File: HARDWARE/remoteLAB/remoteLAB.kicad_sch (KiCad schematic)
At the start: 0 parts

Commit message: add: create schematic files for MCU, TFT, Analog In, Analog Out, Bluetooth, Ethernet, and USBC
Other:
- added sheet Analog input (analog_in.kicad_sch)
- added sheet Analog output (analog_out.kicad_sch)
- added sheet Bluetooth (bluetooth.kicad_sch)
- added sheet Ethernet (ethernet.kicad_sch)
- added sheet MCU (MCU.kicad_sch)
- added sheet TFT (TFT.kicad_sch)
- added sheet USBC (usbc.kicad_sch)

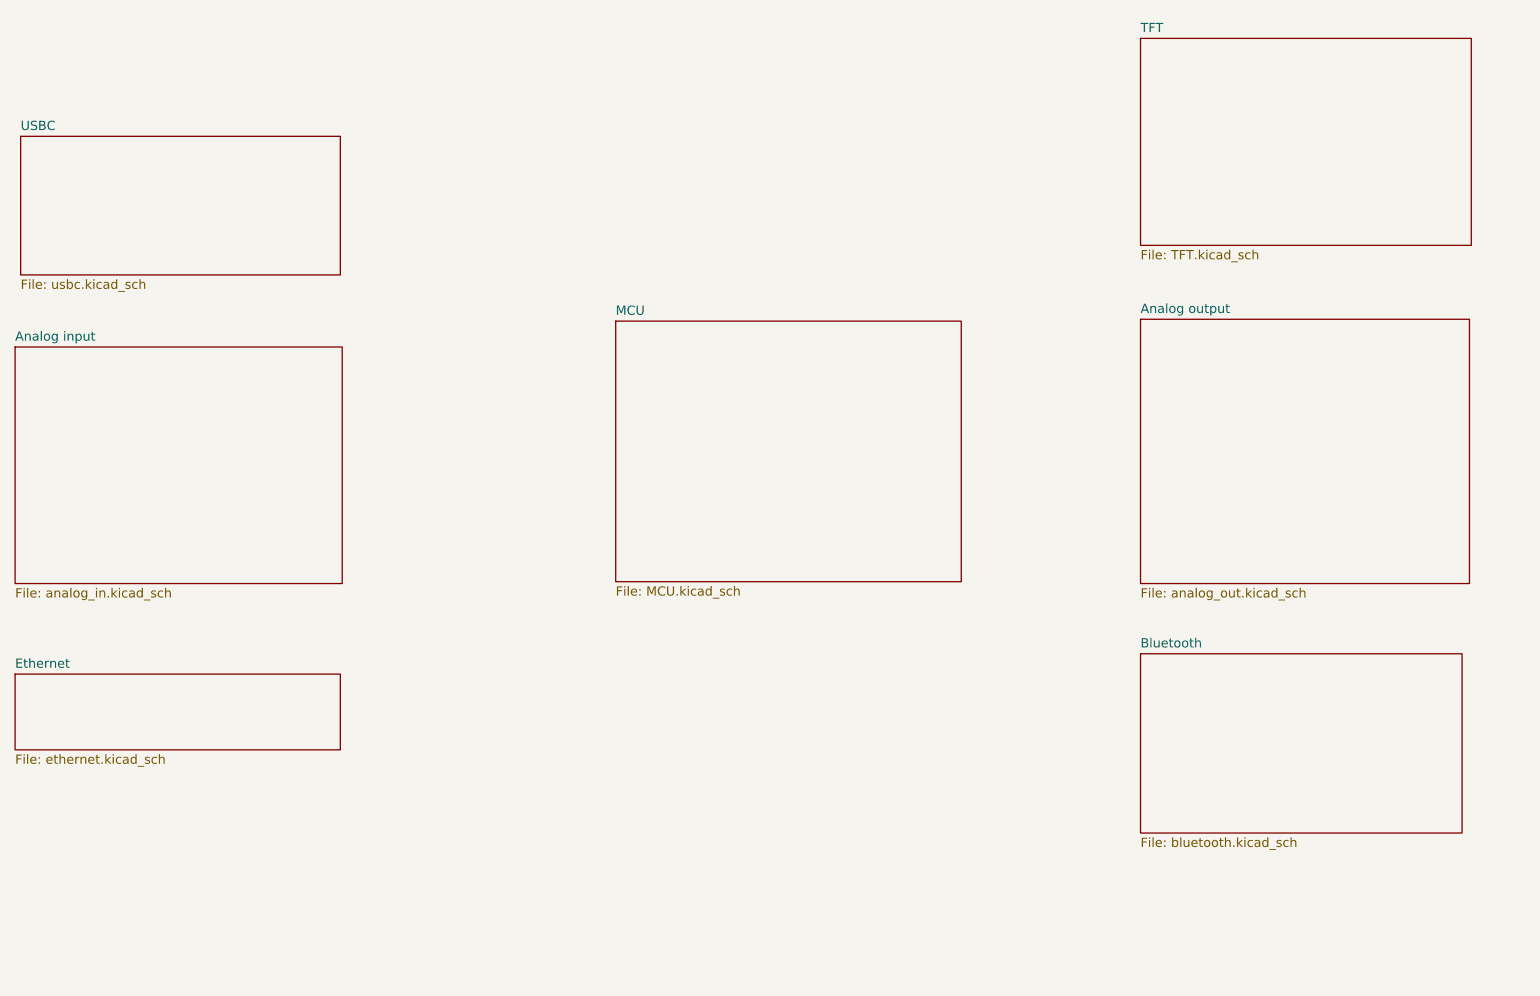
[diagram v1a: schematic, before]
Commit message: added symbols for display connector and BT part, added usb device to ioc
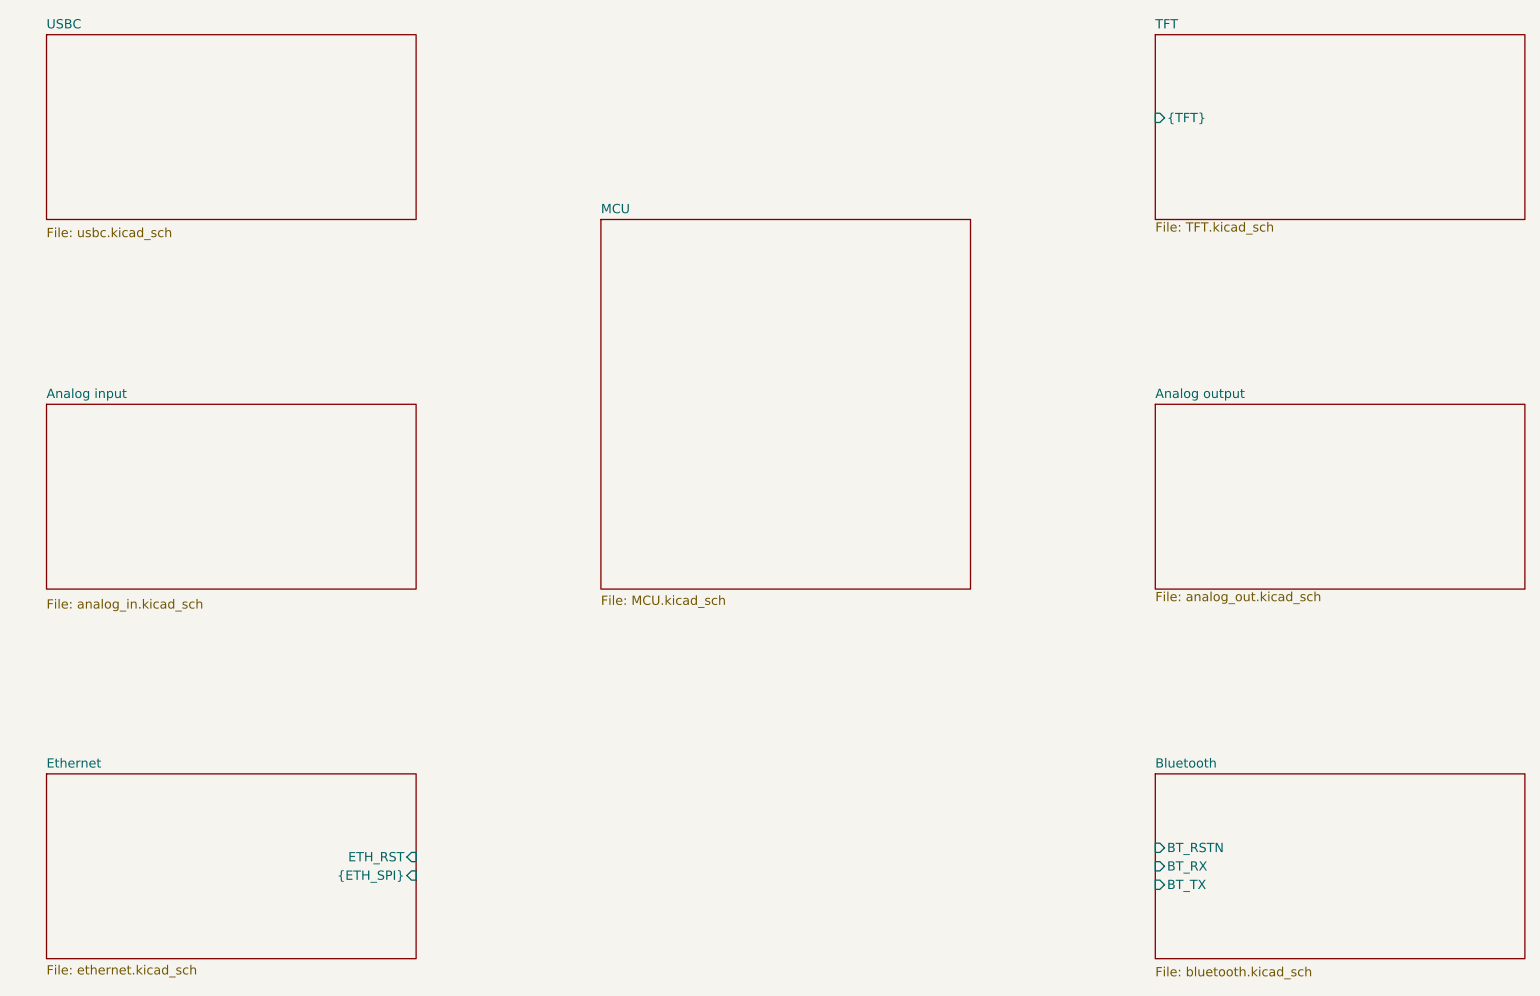
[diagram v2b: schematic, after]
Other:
- sheet Bluetooth ports: added BT_RSTN, BT_RX, BT_TX; removed none
- sheet Ethernet ports: added ETH_RST, {ETH_SPI}; removed none
- sheet TFT ports: added {TFT}; removed none
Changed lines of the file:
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@@
 	(paper "A4")
 	(sheet
-		(at 47.244 39.37)
-		(size 43.942 19.05)
+		(at 50.8 25.4)
+		(size 50.8 25.4)
 		(exclude_from_sim no)
 		(in_bom yes)
@@
 		)
 		(property "Sheetname" "USBC"
-			(at 47.244 38.6584 0)
+			(at 50.8 24.6884 0)
 			(show_name no)
 			(do_not_autoplace no)
@@
 		)
 		(property "Sheetfile" "usbc.kicad_sch"
-			(at 47.244 59.0046 0)
+			(at 50.8 51.8926 0)
 			(show_name no)
 			(do_not_autoplace no)
@@
 	)
 	(sheet
-		(at 201.168 110.49)
-		(size 44.196 24.638)
+		(at 203.2 127)
+		(size 50.8 25.4)
 		(exclude_from_sim no)
 		(in_bom yes)
@@
 		)
 		(property "Sheetname" "Bluetooth"
-			(at 201.168 109.7784 0)
+			(at 203.2 126.2884 0)
 			(show_name no)
 			(do_not_autoplace no)
@@
 		)
 		(property "Sheetfile" "bluetooth.kicad_sch"
-			(at 201.168 135.7126 0)
+			(at 203.2 153.4926 0)
 			(show_name no)
 			(do_not_autoplace no)
@@
 		)
 		(property "Field2" ""
-			(at 201.168 110.49 0)
+			(at 203.2 127 0)
 			(hide yes)
 			(show_name no)
@@
 			)
 		)
+		(pin "BT_RSTN" input
+			(at 203.2 137.16 180)
+			(effects
+				(font
+					(size 1.27 1.27)
+				)
+				(justify left)
+			)
+		)
+		(pin "BT_RX" input
+			(at 203.2 139.7 180)
+			(effects
+				(font
+					(size 1.27 1.27)
+				)
+				(justify left)
+			)
+		)
+		(pin "BT_TX" input
+			(at 203.2 142.24 180)
+			(effects
+				(font
+					(size 1.27 1.27)
+				)
+				(justify left)
+			)
+		)
 		(instances
 			(project "remoteLAB"
@@
 	)
 	(sheet
-		(at 201.168 64.516)
-		(size 45.212 36.322)
+		(at 203.2 76.2)
+		(size 50.8 25.4)
 		(exclude_from_sim no)
 		(in_bom yes)
@@
 		)
 		(property "Sheetname" "Analog output"
-			(at 201.168 63.8044 0)
+			(at 203.2 75.4884 0)
 			(show_name no)
 			(do_not_autoplace no)
@@
 		)
 		(property "Sheetfile" "analog_out.kicad_sch"
-			(at 201.168 101.4226 0)
+			(at 203.2 101.9306 0)
 			(show_name no)
 			(do_not_autoplace no)
@@
 	)
 	(sheet
-		(at 46.482 68.326)
-		(size 44.958 32.512)
+		(at 50.8 76.2)
+		(size 50.8 25.4)
 		(exclude_from_sim no)
 		(in_bom yes)
@@
 		)
 		(property "Sheetname" "Analog input"
-			(at 46.482 67.6144 0)
+			(at 50.8 75.4884 0)
 			(show_name no)
 			(do_not_autoplace no)
@@
 		)
 		(property "Sheetfile" "analog_in.kicad_sch"
-			(at 46.482 101.4226 0)
+			(at 50.8 102.9466 0)
 			(show_name no)
 			(do_not_autoplace no)
@@
 	)
 	(sheet
-		(at 129.032 64.77)
-		(size 47.498 35.814)
+		(at 127 50.8)
+		(size 50.8 50.8)
 		(exclude_from_sim no)
 		(in_bom yes)
@@
 		)
 		(property "Sheetname" "MCU"
-			(at 129.032 64.0584 0)
+			(at 127 50.0884 0)
 			(show_name no)
 			(do_not_autoplace no)
@@
 		)
 		(property "Sheetfile" "MCU.kicad_sch"
-			(at 129.032 101.1686 0)
+			(at 127 102.4386 0)
 			(show_name no)
 			(do_not_autoplace no)
@@
 	)
 	(sheet
-		(at 201.168 25.908)
-		(size 45.466 28.448)
+		(at 203.2 25.4)
+		(size 50.8 25.4)
 		(exclude_from_sim no)
 		(in_bom yes)
@@
 		)
 		(property "Sheetname" "TFT"
-			(at 201.168 25.1964 0)
+			(at 203.2 24.6884 0)
 			(show_name no)
 			(do_not_autoplace no)
@@
 		)
 		(property "Sheetfile" "TFT.kicad_sch"
-			(at 201.168 54.9406 0)
-			(show_name no)
-			(do_not_autoplace no)
-			(effects
-				(font
-					(size 1.27 1.27)
-				)
-				(justify left top)
+			(at 203.2 51.1306 0)
+			(show_name no)
+			(do_not_autoplace no)
+			(effects
+				(font
+					(size 1.27 1.27)
+				)
+				(justify left top)
+			)
+		)
+		(pin "{TFT}" input
+			(at 203.2 36.83 180)
+			(effects
+				(font
+					(size 1.27 1.27)
+				)
+				(justify left)
 			)
 		)
@@
 	)
 	(sheet
-		(at 46.482 113.284)
-		(size 44.704 10.414)
+		(at 50.8 127)
+		(size 50.8 25.4)
 		(exclude_from_sim no)
 		(in_bom yes)
@@
 		)
 		(property "Sheetname" "Ethernet"
-			(at 46.482 112.5724 0)
+			(at 50.8 126.2884 0)
 			(show_name no)
 			(do_not_autoplace no)
@@
 		)
 		(property "Sheetfile" "ethernet.kicad_sch"
-			(at 46.482 124.2826 0)
-			(show_name no)
-			(do_not_autoplace no)
-			(effects
-				(font
-					(size 1.27 1.27)
-				)
-				(justify left top)
-			)
-		)
+			(at 50.8 153.2386 0)
+			(show_name no)
+			(do_not_autoplace no)
+			(effects
+				(font
+					(size 1.27 1.27)
+				)
+				(justify left top)
+			)
+		)
+		(pin "ETH_RST" input
+			(at 101.6 138.43 0)
+			(effects
+				(font
+					(size 1.27 1.27)
+				)
+				(justify right)
+			)
+		)
+		(pin "{ETH_SPI}" input
+			(at 101.6 140.97 0)
+			(effects
+				(font
+					(size 1.27 1.27)
+				)
+				(justify right)
+			)
+		)

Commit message: usb power isolation and input
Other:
- sheet USBC ports: added DD+, DD-; removed none
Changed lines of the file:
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@@
+			)
+		)
+		(pin "DD+" input
+			(at 101.6 34.29 0)
+			(effects
+				(font
+					(size 1.27 1.27)
+				)
+				(justify right)
+			)
+		)
+		(pin "DD-" input
+			(at 101.6 36.83 0)
+			(effects
+				(font
+					(size 1.27 1.27)
+				)
+				(justify right)
 			)
 		)
